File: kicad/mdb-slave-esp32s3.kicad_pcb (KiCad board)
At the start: 2 copper layers, 39 x 41 mm, 40 parts, among them J1 MDB_Connector, J2 USB_C_Receptacle_USB2.0_16P, J3 Conn_02x11_Odd_Even, SW1 SW_Push, U1 TLP785, U3 ESP32-S3FH4R2, U4 TLP785, U5 LM2594HVM-3.3, Y1 Crystal_GND24

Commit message: Fixing usb-c <-> usb-c communication error: Resistor 10k -> 5.1k
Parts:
- R7, R8: value 10k -> 5.1k
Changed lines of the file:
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@@
 			)
 		)
-		(property "Value" "10k"
+		(property "Value" "5.1k"
 			(at 0 1.43 90)
 			(layer "F.Fab")
@@
 			)
 		)
-		(property "Value" "10k"
+		(property "Value" "5.1k"
 			(at 0 1.43 90)
 			(layer "F.Fab")
@@
 			)
 		)
-		(property "LCSC#" "C98220"
+		(property "LCSC#" "C394543"
 			(at 0 0 90)
 			(unlocked yes)
@@
 	)
 	(zone
-		(net 3)
-		(net_name "GND")
-		(layer "F.Cu")
-		(name "$teardrop_padvia$")
-		(hatch none 0.1)
-		(priority 30013)
-		(attr
-			(teardrop
-				(type padvia)
-			)
-		)
-		(connect_pads yes
-			(clearance 0)
-		)
-		(min_thickness 0.0254)
-		(filled_areas_thickness no)
-		(fill yes
-			(thermal_gap 0.5)
-			(thermal_bridge_width 0.5)
-			(island_removal_mode 1)
-			(island_area_min 10)
-		)
-		(polygon
-			(pts
-				(xy 180.271701 121.773876) (xy 180.413123 121.915298) (xy 181.028825 121.865279) (xy 181.187706 120.999293)
-				(xy 180.686999 120.792893)
-			)
-		)
-	)
-	(zone
 		(net 7)
 		(net_name "/vin")
@@
 		(name "$teardrop_padvia$")
 		(hatch none 0.1)
-		(priority 30011)
-		(attr
-			(teardrop
-				(type padvia)
-			)
-		)
-		(connect_pads yes
-			(clearance 0)
-		)
-		(min_thickness 0.0254)
-		(filled_areas_thickness no)
-		(fill yes
-			(thermal_gap 0.5)
-			(thermal_bridge_width 0.5)
-			(island_removal_mode 1)
-			(island_area_min 10)
-		)
-		(polygon
-			(pts
-				(xy 182.145578 116.45) (xy 182.145578 115.95) (xy 181.588899 115.95838) (xy 181.185999 116.8) (xy 181.686999 117.076434)
-			)
-		)
-	)
-	(zone
-		(net 3)
-		(net_name "GND")
-		(layer "F.Cu")
-		(name "$teardrop_padvia$")
-		(hatch none 0.1)
-		(priority 30012)
+		(priority 30001)
 		(attr
 			(teardrop
@@
 		(name "$teardrop_padvia$")
 		(hatch none 0.1)
+		(priority 30002)
+		(attr
+			(teardrop
+				(type padvia)
+			)
+		)
+		(connect_pads yes
+			(clearance 0)
+		)
+		(min_thickness 0.0254)
+		(filled_areas_thickness no)
+		(fill yes
+			(thermal_gap 0.5)
+			(thermal_bridge_width 0.5)
+			(island_removal_mode 1)
+			(island_area_min 10)
+		)
+		(polygon
+			(pts
+				(xy 180.271701 121.773876) (xy 180.413123 121.915298) (xy 181.028825 121.865279) (xy 181.187706 120.999293)
+				(xy 180.686999 120.792893)
+			)
+		)
+	)
+	(zone
+		(net 3)
+		(net_name "GND")
+		(layer "F.Cu")
+		(name "$teardrop_padvia$")
+		(hatch none 0.1)
 		(priority 30014)
 		(attr
@@
 	)
 	(zone
+		(net 3)
+		(net_name "GND")
+		(layer "F.Cu")
+		(name "$teardrop_padvia$")
+		(hatch none 0.1)
+		(priority 30000)
+		(attr
+			(teardrop
+				(type padvia)
+			)
+		)
+		(connect_pads yes
+			(clearance 0)
+		)
+		(min_thickness 0.0254)
+		(filled_areas_thickness no)
+		(fill yes
+			(thermal_gap 0.5)
+			(thermal_bridge_width 0.5)
+			(island_removal_mode 1)
+			(island_area_min 10)
+		)
+		(polygon
+			(pts
+				(xy 182.145578 116.45) (xy 182.145578 115.95) (xy 181.588899 115.95838) (xy 181.185999 116.8) (xy 181.686999 117.076434)
+			)
+		)
+	)
+	(zone
 		(net 7)
 		(net_name "/vin")
@@
 	)
 	(zone
+		(net 3)
+		(net_name "GND")
+		(layer "B.Cu")
+		(name "$teardrop_padvia$")
+		(hatch none 0.1)
+		(priority 30005)
+		(attr
+			(teardrop
+				(type padvia)
+			)
+		)
+		(connect_pads yes
+			(clearance 0)
+		)
+		(min_thickness 0.0254)
+		(filled_areas_thickness no)
+		(fill yes
+			(thermal_gap 0.5)
+			(thermal_bridge_width 0.5)
+			(island_removal_mode 1)
+			(island_area_min 10)
+		)
+		(polygon
+			(pts
+				(xy 188.826999 120.75) (xy 188.826999 121.25) (xy 189.337623 121.5) (xy 189.827999 121) (xy 189.337623 120.5)
+			)
+		)
+	)
+	(zone
 		(net 2)
 		(net_name "+3V3")
@@
 		(name "$teardrop_padvia$")
 		(hatch none 0.1)
-		(priority 30003)
+		(priority 30000)
 		(attr
 			(teardrop
@@
 		(name "$teardrop_padvia$")
 		(hatch none 0.1)
-		(priority 30005)
+		(priority 30001)
 		(attr
 			(teardrop
@@
 		(polygon
 			(pts
-				(xy 190.076999 119.609607) (xy 189.576999 119.609607) (xy 189.336606 120.502455) (xy 189.826999 121.001)
-				(xy 190.317392 120.502455)
+				(xy 189.576999 118.340393) (xy 190.076999 118.340393) (xy 190.317392 117.447545) (xy 189.826999 116.799)
+				(xy 189.336606 117.447545)
 			)
 		)
@@
 	)
 	(zone
-		(net 2)
-		(net_name "+3V3")
+		(net 3)
+		(net_name "GND")
 		(layer "B.Cu")
 		(name "$teardrop_padvia$")
 		(hatch none 0.1)
-		(priority 30017)
+		(priority 30002)
 		(attr
 			(teardrop
@@
 		(polygon
 			(pts
-				(xy 191.64 104.991568) (xy 192.14 104.991568) (xy 191.692588 104.187772) (xy 191.36 104.409) (xy 191.137772 104.742588)
+				(xy 181.436999 119.609607) (xy 180.936999 119.609607) (xy 180.696606 120.502455) (xy 181.186999 121.001)
+				(xy 181.677392 120.502455)
 			)
 		)
 	)
 	(zone
-		(net 3)
-		(net_name "GND")
+		(net 2)
+		(net_name "+3V3")
 		(layer "B.Cu")
 		(name "$teardrop_padvia$")
 		(hatch none 0.1)
-		(priority 30002)
+		(priority 30017)
 		(attr
 			(teardrop
@@
 		(polygon
 			(pts
-				(xy 176.883667 114.18) (xy 176.883667 113.98) (xy 175.672235 113.373251) (xy 175.199 114.08) (xy 175.672235 114.786749)
+				(xy 191.64 104.991568) (xy 192.14 104.991568) (xy 191.692588 104.187772) (xy 191.36 104.409) (xy 191.137772 104.742588)
 			)
 		)
@@
 		(name "$teardrop_padvia$")
 		(hatch none 0.1)
-		(priority 30007)
+		(priority 30002)
 		(attr
 			(teardrop
@@
 		(polygon
 			(pts
-				(xy 182.186999 121.25) (xy 182.186999 120.75) (xy 181.676375 120.5) (xy 181.185999 121) (xy 181.676375 121.5)
+				(xy 176.883667 114.18) (xy 176.883667 113.98) (xy 175.672235 113.373251) (xy 175.199 114.08) (xy 175.672235 114.786749)
 			)
 		)
@@
 		(name "$teardrop_padvia$")
 		(hatch none 0.1)
-		(priority 30006)
+		(priority 30003)
 		(attr
 			(teardrop
@@
 		(polygon
 			(pts
-				(xy 181.436999 119.609607) (xy 180.936999 119.609607) (xy 180.696606 120.502455) (xy 181.186999 121.001)
-				(xy 181.677392 120.502455)
+				(xy 190.076999 119.609607) (xy 189.576999 119.609607) (xy 189.336606 120.502455) (xy 189.826999 121.001)
+				(xy 190.317392 120.502455)
 			)
 		)
@@
 		(name "$teardrop_padvia$")
 		(hatch none 0.1)
-		(priority 30012)
+		(priority 30004)
 		(attr
 			(teardrop
@@
 		(polygon
 			(pts
-				(xy 190.227686 106.14) (xy 190.227686 106.64) (xy 190.941964 106.782314) (xy 191.021 106.39) (xy 190.941964 105.997686)
+				(xy 182.186999 121.25) (xy 182.186999 120.75) (xy 181.676375 120.5) (xy 181.185999 121) (xy 181.676375 121.5)
 			)
 		)
@@
 		(name "$teardrop_padvia$")
 		(hatch none 0.1)
-		(priority 30004)
+		(priority 30012)
 		(attr
 			(teardrop
@@
 		(polygon
 			(pts
-				(xy 189.576999 118.340393) (xy 190.076999 118.340393) (xy 190.317392 117.447545) (xy 189.826999 116.799)
-				(xy 189.336606 117.447545)
+				(xy 190.227686 106.14) (xy 190.227686 106.64) (xy 190.941964 106.782314) (xy 191.021 106.39) (xy 190.941964 105.997686)
 			)
 		)
@@
 			)
 		)
-	)
-	(zone
-		(net 3)
-		(net_name "GND")
-		(layer "B.Cu")
-		(name "$teardrop_padvia$")
-		(hatch none 0.1)
-		(priority 30008)
-		(attr
-			(teardrop
-				(type padvia)
-			)
-		)
-		(connect_pads yes
-			(clearance 0)
-		)
-		(min_thickness 0.0254)
-		(filled_areas_thickness no)
-		(fill yes
-			(thermal_gap 0.5)
-			(thermal_bridge_width 0.5)
-			(island_removal_mode 1)
-			(island_area_min 10)
-		)
-		(polygon
-			(pts
-				(xy 188.826999 120.75) (xy 188.826999 121.25) (xy 189.337623 121.5) (xy 189.827999 121) (xy 189.337623 120.5)
-			)
-		)

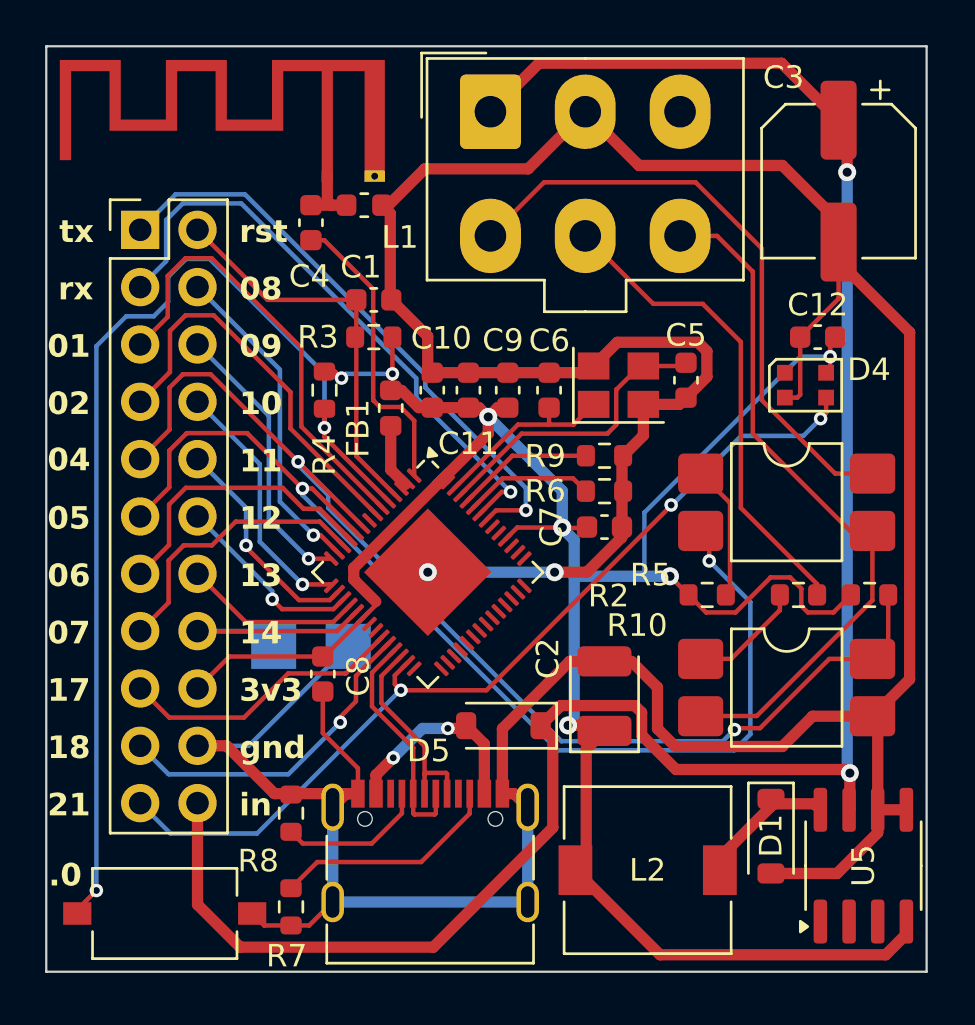
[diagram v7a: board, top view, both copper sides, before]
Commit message: Updating optoacoplator package SOP-4_2.54
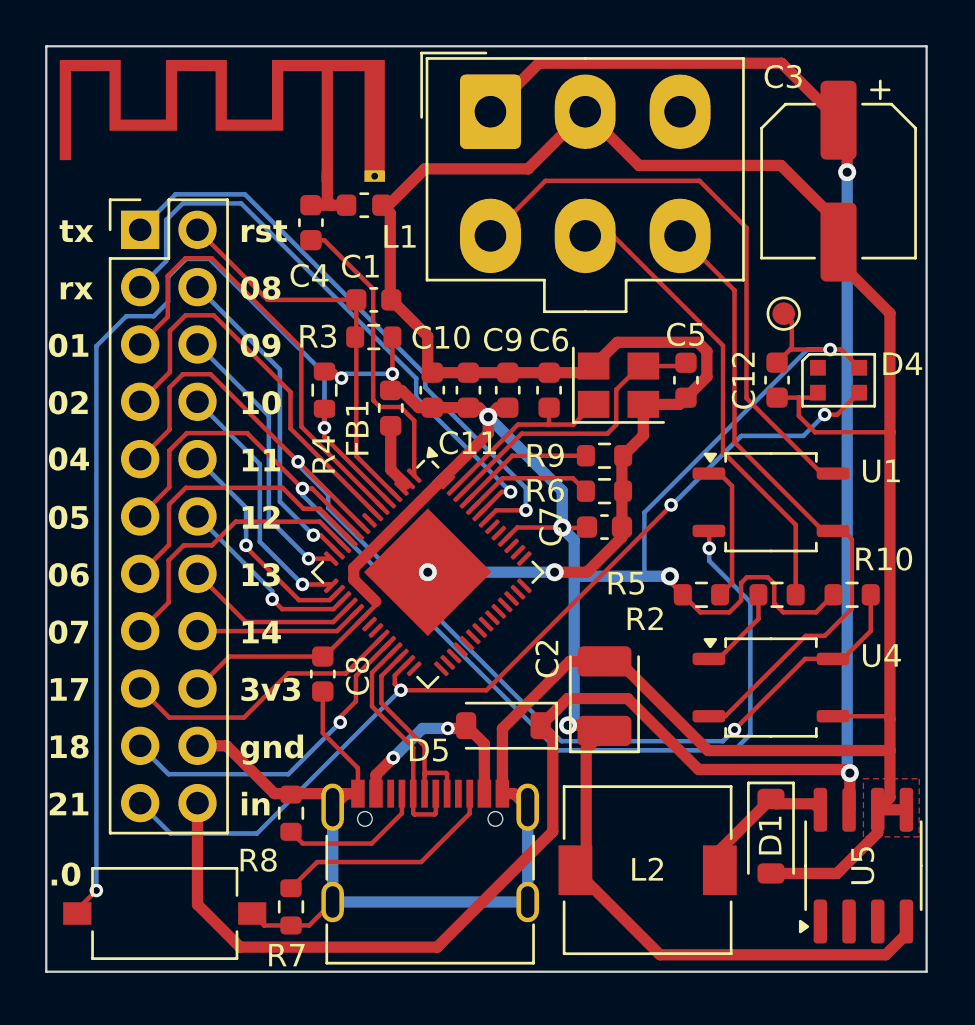
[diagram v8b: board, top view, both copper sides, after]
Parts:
- removed TP1: Buzzer_Flag (14), TestPoint:TestPoint_Pad_2.0x2.0mm
- removed TP2: Buzzer_Flag (-), TestPoint:TestPoint_Pad_2.0x2.0mm
- added TP4: TestPoint, TestPoint:TestPoint_Pad_D1.0mm, F.Cu at (201.2, 94.9)
- U1, U4: footprint Package_DIP:SMDIP-4_W7.62mm -> Package_SO:SOP-4_3.8x4.1mm_P2.54mm
- moved C12 2.62 mm to (200.9, 97.9), turned to 90 degrees
- moved D4 1.48 mm to (203.6, 97.9)
- moved R2 0.95 mm to (200.9, 107.4)
- moved REF** 0.94 mm to (192.4, 103.6)
- moved R10 0.78 mm to (204.2, 107.4)
- moved U1 0.69 mm to (200.6, 103.3)
- moved U4 0.69 mm to (200.6, 111.5)
- moved R5 0.26 mm to (197.5, 107.4)
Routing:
- net GND: track 178.6 -> 169.8 mm
- net +3V3: track 108.0 -> 112.2 mm
- net /io14: track 11.1 -> 7.42 mm
- net /mdb_communications_common: track 31.0 -> 28.5 mm
- net /mdb_master_receive: track 27.2 -> 26.0 mm
- net /io21: track 40.9 -> 42.1 mm
- net /io4: track 51.0 -> 49.9 mm
- net Net-(R2-Pad2): track 5.08 -> 4.00 mm
- net /mdb_master_transmit: track 21.4 -> 20.5 mm
- added copper zone on F.Cu, net GND
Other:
- board text removed: "io14"
